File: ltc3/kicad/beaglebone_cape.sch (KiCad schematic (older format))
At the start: 8 parts, among them U501 24C256

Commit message: LTC3: Cleaned up battery charging and BeagleBone interface sheets.
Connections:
- net DC_3.3V: no longer names the net of C501.3 (DC_3.3V)
- net DC_3.3V: no longer C501.4 (DC_3.3V)
- net I2C2_SCL: no longer names the net of C501.19 (D17/I2C2_SCL), R501.2, U501.6 (SCL)
- net I2C2_SDA: no longer names the net of C501.20 (D18/I2C2_SDA), R502.2, U501.5 (SDA)
- net SYS_5V: no longer names the net of C501.7 (SYS_5V)
- net SYS_5V: no longer C501.8 (SYS_5V)
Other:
- moved on the sheet: C501A, C501B, C502, JP501, R501, R502, R503, R504, U501

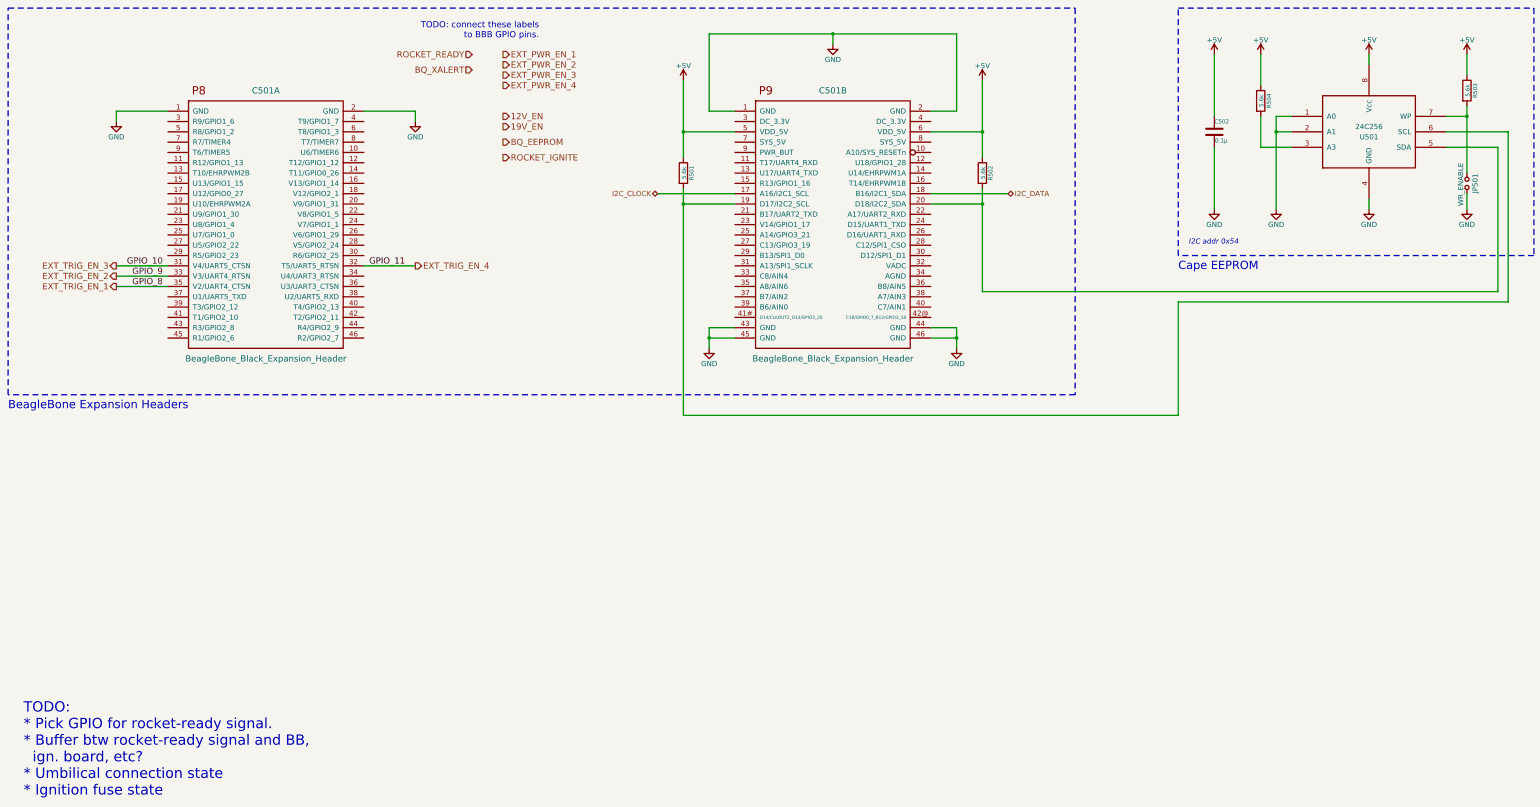
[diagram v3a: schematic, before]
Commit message: Selected GPIO Pins for unassigned signals on BBB.  Added Notes to BBB Sheet.
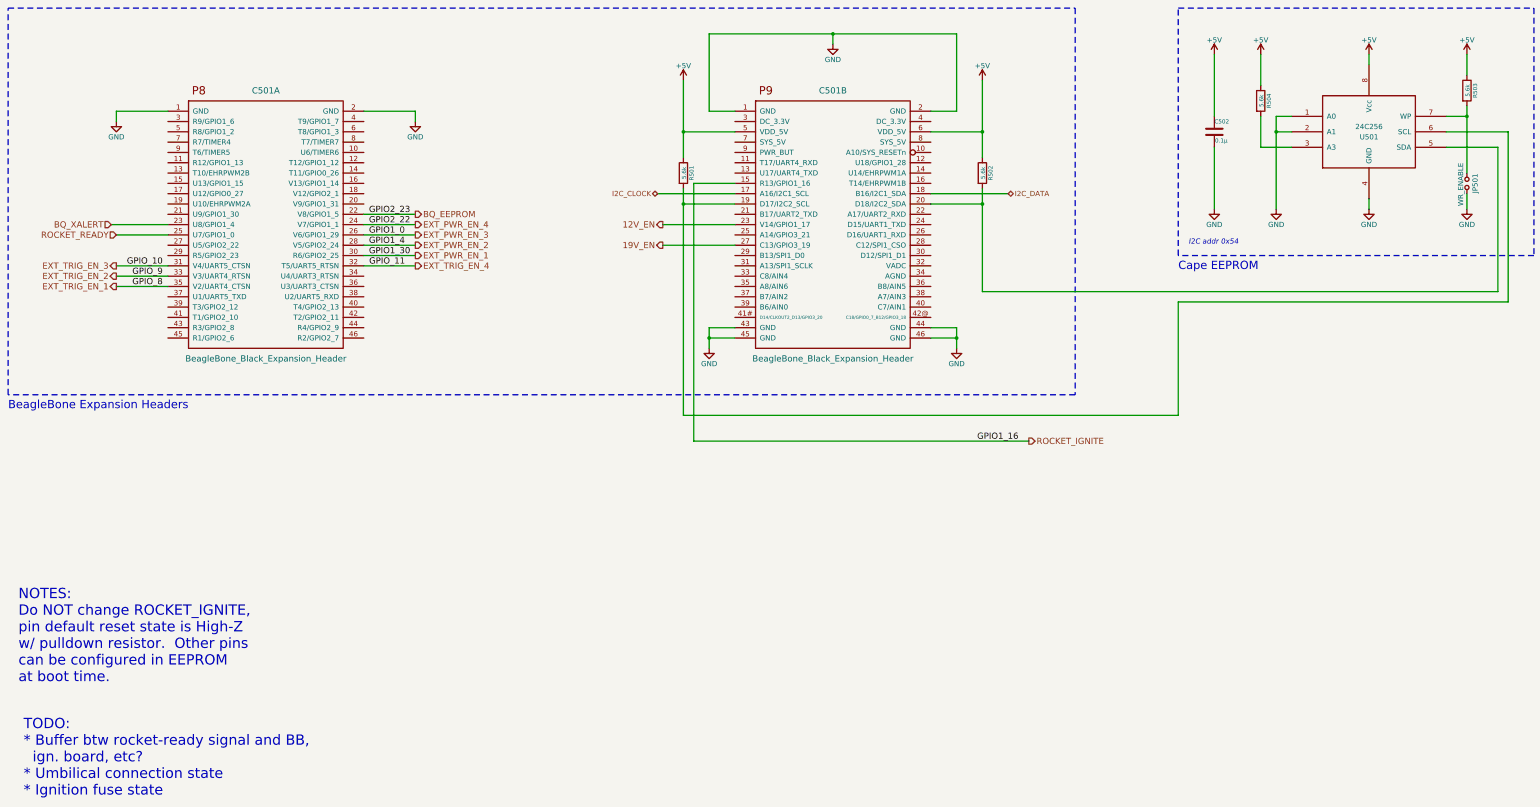
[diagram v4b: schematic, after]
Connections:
- net 12V_EN: now also C501.23 (V14/GPIO1_17)
- net 19V_EN: now also C501.27 (C13/GPIO3_19)
- net BQ_EEPROM: now also C501.22 (V8/GPIO1_5)
- net BQ_XALERT: now also C501.23 (U8/GPIO1_4)
- net EXT_PWR_EN_1: now also C501.30 (R6/GPIO2_25)
- net EXT_PWR_EN_2: now also C501.28 (V5/GPIO2_24)
- net EXT_PWR_EN_3: now also C501.26 (V6/GPIO1_29)
- net EXT_PWR_EN_4: now also C501.24 (V7/GPIO1_1)
- net ROCKET_IGNITE: now also C501.15 (R13/GPIO1_16)
- net ROCKET_READY: now also C501.25 (U7/GPIO1_0)
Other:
- note added: "NOTES:\nDo NOT change ROCKET_IGNITE, \npin default reset state is High-Z \nw/ pulldown resistor. Other pins\ncan be configured in EEPROM\nat boot time."
- note added: "TODO:\n* Buffer btw rocket-ready signal and BB,\n ign. board, etc?\n* Umbilical connection state\n* Ignition fuse state"
- note removed: "TODO: connect these labels\nto BBB GPIO pins."
- note removed: "TODO:\n* Pick GPIO for rocket-ready signal.\n* Buffer btw rocket-ready signal and BB,\n ign. board, etc?\n* Umbilical connection state\n* Ignition fuse state"
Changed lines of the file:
@@
 Text HLabel 4900 4850 2    60   Output ~ 0
 EXT_TRIG_EN_4
-Text HLabel 5750 2800 2    60   Output ~ 0
+Text HLabel 4900 4750 2    60   Output ~ 0
 EXT_PWR_EN_1
-Text HLabel 5750 2900 2    60   Output ~ 0
+Text HLabel 4900 4650 2    60   Output ~ 0
 EXT_PWR_EN_2
-Text HLabel 5750 3000 2    60   Output ~ 0
+Text HLabel 4900 4550 2    60   Output ~ 0
 EXT_PWR_EN_3
-Text HLabel 5750 3100 2    60   Output ~ 0
+Text HLabel 4900 4450 2    60   Output ~ 0
 EXT_PWR_EN_4
-Text Notes 6100 2650 2    60   ~ 0
-TODO: connect these labels\nto BBB GPIO pins.
 $Comp
 L GND #PWR514
@@
 $EndComp
 Text Notes 1100 10000 0    100  ~ 0
-TODO:\n* Pick GPIO for rocket-ready signal.\n* Buffer btw rocket-ready signal and BB,\n  ign. board, etc?\n* Umbilical connection state\n* Ignition fuse state
-Text HLabel 5750 3400 2    60   Output ~ 0
+TODO:\n* Buffer btw rocket-ready signal and BB,\n  ign. board, etc?\n* Umbilical connection state\n* Ignition fuse state
+Text HLabel 7300 4450 0    60   Output ~ 0
 12V_EN
-Text HLabel 5750 3500 2    60   Output ~ 0
+Text HLabel 7300 4650 0    60   Output ~ 0
 19V_EN
 Wire Notes Line
@@
 	14900 3550 15500 3550
 Wire Wire Line
-	15100 3300 15100 3400
-Wire Wire Line
-	15100 3400 15100 3950
+	15100 3300 15100 3950
 Wire Wire Line
 	14900 3400 15100 3400
@@
 	13400 3550 13250 3550
 Wire Wire Line
-	13250 3400 13250 3550
-Wire Wire Line
-	13250 3550 13250 4300
+	13250 3400 13250 4300
 Wire Wire Line
 	13400 3400 13250 3400
@@
 $EndComp
 Wire Wire Line
-	7750 5450 7750 5550
-Wire Wire Line
-	7750 5550 7750 5650
+	7750 5450 7750 5650
 Wire Wire Line
 	7750 5550 8000 5550
@@
 $EndComp
 Wire Wire Line
-	10150 5450 10150 5550
-Wire Wire Line
-	10150 5550 10150 5650
+	10150 5450 10150 5650
 Wire Wire Line
 	10150 5550 9900 5550
@@
 	7750 3350 7750 2600
 Wire Wire Line
-	7750 2600 8950 2600
-Wire Wire Line
-	8950 2600 10150 2600
+	7750 2600 10150 2600
 Wire Wire Line
 	8950 2600 8950 2700
@@
 	1    0    0    -1
 $EndComp
-Text HLabel 5450 2800 0    60   Input ~ 0
+Text HLabel 2000 4550 0    60   Input ~ 0
 ROCKET_READY
 $Comp
@@
 $EndComp
 Wire Wire Line
-	10400 3050 10400 3550
-Wire Wire Line
-	10400 3550 10400 3800
+	10400 3050 10400 3800
 $Comp
 L +5V #PWR502
@@
 $EndComp
 Wire Wire Line
-	7500 3050 7500 3550
-Wire Wire Line
-	7500 3550 7500 3800
+	7500 3050 7500 3800
 $Comp
 L +5V #PWR508
@@
 Connection ~ 7500 3550
 Wire Wire Line
-	7500 4100 7500 4250
-Wire Wire Line
-	7500 4250 7500 6300
+	7500 4100 7500 6300
 Wire Wire Line
 	7500 4250 8000 4250
 Connection ~ 10400 3550
 Wire Wire Line
-	10400 4100 10400 4250
-Wire Wire Line
-	10400 4250 10400 5100
+	10400 4100 10400 5100
 Wire Notes Line
 	950  2350 11300 2350
@@
 Text HLabel 10650 4150 2    50   BiDi ~ 0
 I2C_DATA
-Text HLabel 5450 2950 0    60   Input ~ 0
+Text HLabel 1950 4450 0    60   Input ~ 0
 BQ_XALERT
-Text HLabel 5750 3650 2    60   Output ~ 0
+Text HLabel 4900 4350 2    60   Output ~ 0
 BQ_EEPROM
-Text HLabel 5750 3800 2    60   Output ~ 0
+Text HLabel 10850 6550 2    60   Output ~ 0
 ROCKET_IGNITE
 Wire Wire Line
@@
 	12300 5200 12300 6300
 Connection ~ 7500 4250
+Wire Wire Line
+	8000 4050 7600 4050
+Wire Wire Line
+	7600 4050 7600 6550
+Wire Wire Line
+	7600 6550 10850 6550
+Wire Wire Line
+	4400 4550 4900 4550
+Wire Wire Line
+	4400 4350 4900 4350
+Wire Wire Line
+	4400 4650 4900 4650
+Wire Wire Line
+	4400 4750 4900 4750
+Wire Wire Line
+	4400 4450 4900 4450
+Text Label 4450 4350 0    60   ~ 0
+GPIO2_23
+Text Label 4450 4450 0    60   ~ 0
+GPIO2_22
+Text Label 4450 4550 0    60   ~ 0
+GPIO1_0
+Text Label 4450 4650 0    60   ~ 0
+GPIO1_4
+Text Label 4450 4750 0    60   ~ 0
+GPIO1_30
+Text Label 10750 6550 2    60   ~ 0
+GPIO1_16
+Wire Wire Line
+	2500 4550 2000 4550
+Wire Wire Line
+	2500 4450 1950 4450
+Wire Wire Line
+	7300 4450 8000 4450
+Wire Wire Line
+	8000 4650 7300 4650
+Text Notes 1050 8900 0    100  ~ 0
+NOTES:\nDo NOT change ROCKET_IGNITE, \npin default reset state is High-Z \nw/ pulldown resistor.  Other pins\ncan be configured in EEPROM\nat boot time.
 $EndSCHEMATC

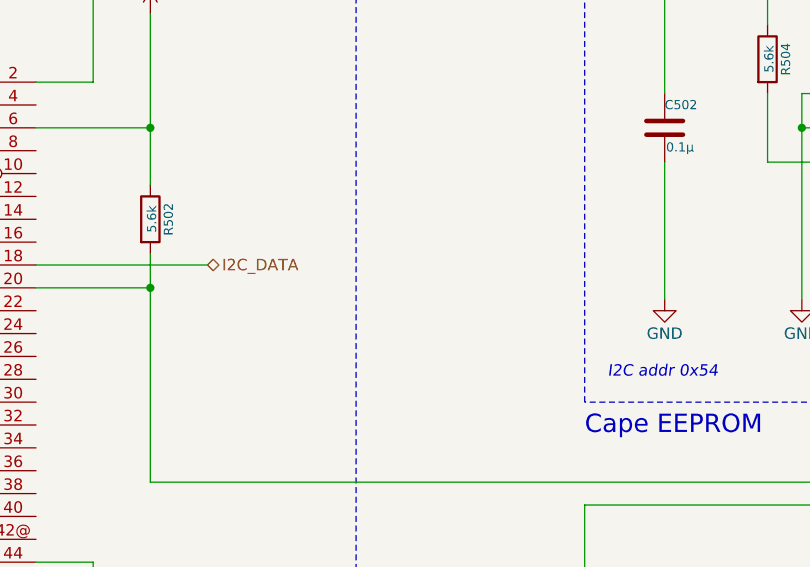
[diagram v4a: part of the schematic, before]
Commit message: LTC3: Added TODO notes to schematic; added questions for upcoming design review.
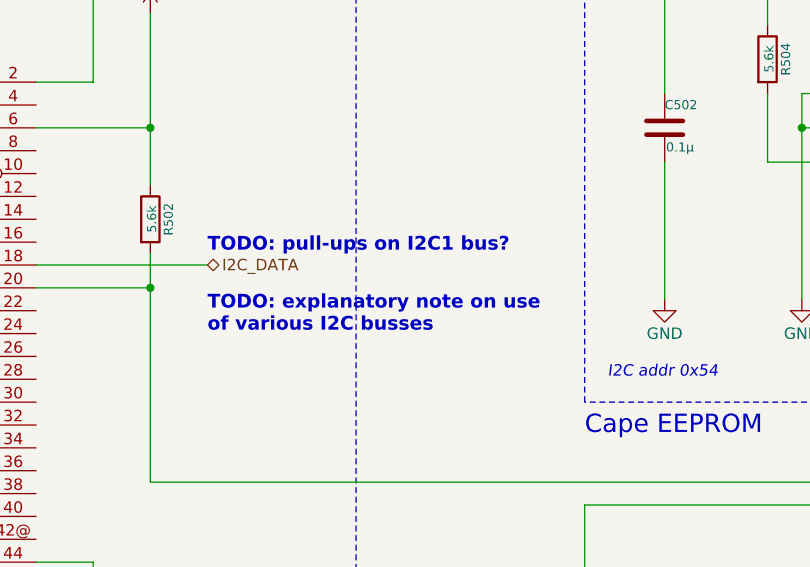
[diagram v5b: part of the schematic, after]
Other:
- note added: "TODO: explanatory note on use\nof various I2C busses"
- note added: "TODO: pull-ups on I2C1 bus?"
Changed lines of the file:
@@
 Text Notes 1050 8900 0    100  ~ 0
 NOTES:\nDo NOT change ROCKET_IGNITE, \npin default reset state is High-Z \nw/ pulldown resistor.  Other pins\ncan be configured in EEPROM\nat boot time.
+Text Notes 10650 4100 0    60   ~ 12
+TODO: pull-ups on I2C1 bus?
+Text Notes 10650 4450 0    60   ~ 12
+TODO: explanatory note on use\nof various I2C busses
 $EndSCHEMATC

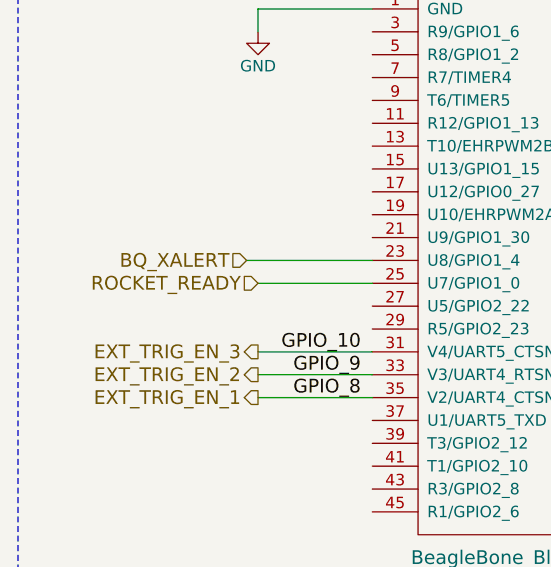
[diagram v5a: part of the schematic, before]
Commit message: LTC3: Minor progress on ignition schematic.
1. Corrected BBB ROCKET_READY signal (prefixed w/ slash to indicate
active-low).

2. Added explanatory note to ignition schematic's "Input Logic" block.

3. More TODOs, comments added to schematic; more questions added to
DESIGN_REVIEW_QUESTIONS list.

4. Updated schematic PDF.
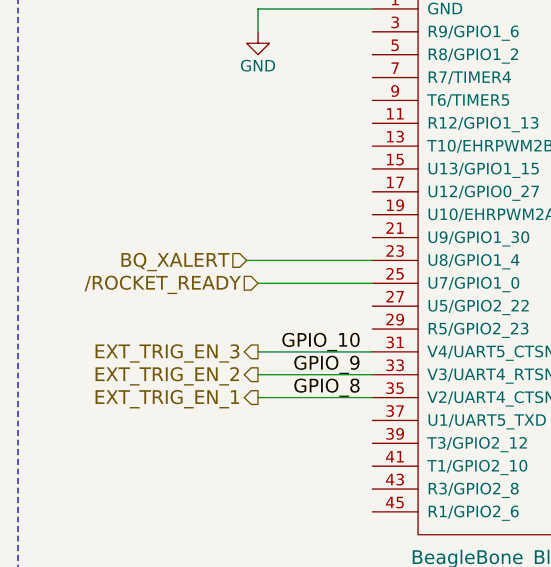
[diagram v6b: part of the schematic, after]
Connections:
- net ROCKET_READY renamed /ROCKET_READY
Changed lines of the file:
@@
 Sheet 5 7
 Title "LTC3 BeagleBone Black Cape Interface"
-Date "2016-01-16"
+Date "2016-01-30"
 Rev "A"
 Comp "Portland State Aerospace Society <http://psas.pdx.edu/>"
@@
 $EndComp
 Text HLabel 2000 4550 0    60   Input ~ 0
-ROCKET_READY
+/ROCKET_READY
 $Comp
 L +5V #PWR503

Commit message: LTC3: Minor adjustments, many comments from today's design review.
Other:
- note added: "TODO: 41#? 42@?"
- note added: "TODO: I2C2 label"
- note added: "TODO: pull-ups on I2C1 lines?\nNo-place pull-ups."
- note added: "TODO:\n* Umbilical connection state\n* Ignition fuse state\n* Table of I2C bus address assignments"
- note removed: "TODO:\n* Buffer btw rocket-ready signal and BB,\n ign. board, etc?\n* Umbilical connection state\n* Ignition fuse state"
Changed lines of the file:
@@
 LIBS:NDS9407
 LIBS:PI2127
-LIBS:Launch_Tower_Computer_III-cache
 EELAYER 25 0
 EELAYER END
@@
 Sheet 5 7
 Title "LTC3 BeagleBone Black Cape Interface"
-Date "2016-01-30"
+Date "2016-02-06"
 Rev "A"
 Comp "Portland State Aerospace Society <http://psas.pdx.edu/>"
@@
 $EndComp
 Text Notes 1100 10000 0    100  ~ 0
-TODO:\n* Buffer btw rocket-ready signal and BB,\n  ign. board, etc?\n* Umbilical connection state\n* Ignition fuse state
+TODO:\n* Umbilical connection state\n* Ignition fuse state\n* Table of I2C bus address assignments
 Text HLabel 7300 4450 0    60   Output ~ 0
 12V_EN
@@
 Text Notes 10650 4450 0    60   ~ 12
 TODO: explanatory note on use\nof various I2C busses
+Text Notes 15250 3500 0    80   ~ 16
+TODO: I2C2 label
+Text Notes 6300 5400 0    80   ~ 16
+TODO: 41#? 42@?
+Text Notes 5900 5000 0    80   ~ 16
+TODO: pull-ups on I2C1 lines?\nNo-place pull-ups.
 $EndSCHEMATC
